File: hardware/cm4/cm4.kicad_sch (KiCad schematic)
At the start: 10 parts, among them J11 CM4 Stecker 1, J12 CM4 Stecker 2, Q10 BSS84

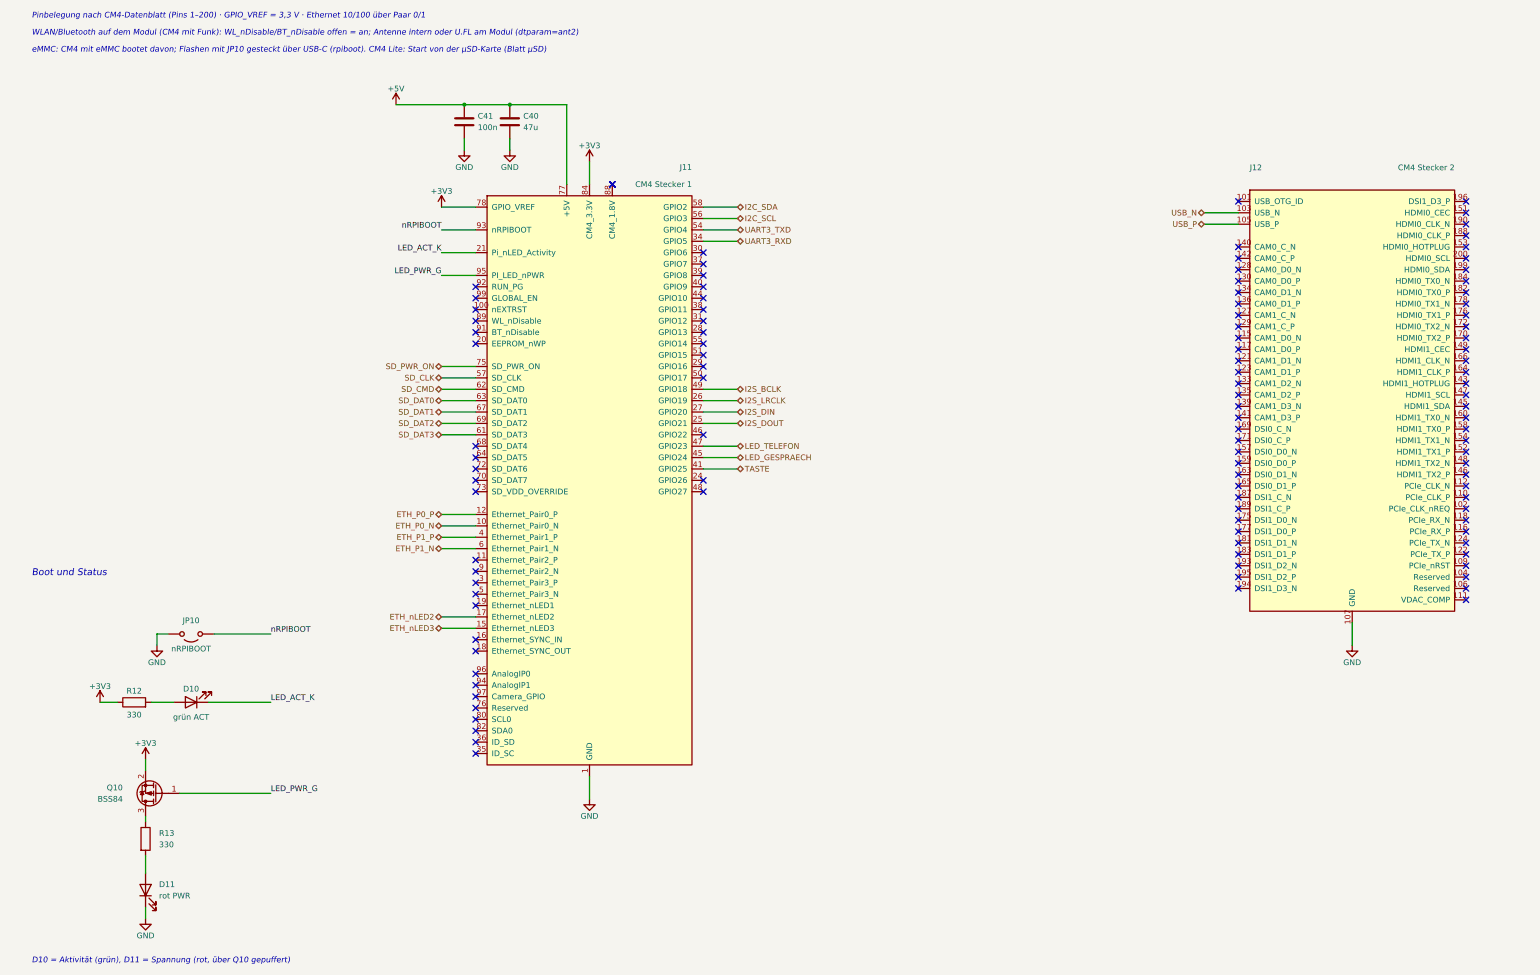
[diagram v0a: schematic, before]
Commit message: CM4-Träger 0.3: Leiterplatte (4 Lagen, JLCPCB), Ein/Aus-Taster, Lüfter, lieferbare Teile
Schaltplan
- Codec TI TLV320AIC3204 statt WM8731 (abgekündigt); MCLK 12 MHz, Reset GPIO26, I²C an GPIO0/1
- Ein/Aus-Taster an GPIO3 (gpio-shutdown im Betrieb, Bootloader-Wecken im Halt)
- Lüfterblatt: AO3400A an GPIO12, Freilaufdiode, JST-PH-Anschluss; gpio-fan über SoC-Temperatur
- Konfig-Taster SW2 und Status-LED D3; Würth RJ45/RJ12, Bourns SM-LP-5001, TPD4E05U06
- reproduzierbare UUIDs (Schaltplan ↔ Platine bleiben verknüpft), eigene Footprints in hardware/bibliothek

Leiterplatte (erzeuge_layout.py)
- 110 × 85 mm, F.Cu / In1 GND / In2 +3V3 / B.Cu, JLC04161H-7628, JLCPCB-Regeln (.kicad_dru)
- CM4-Lage nach CM4IO-Referenz, Antennen-Sperrzone, isolierte Bereiche GND_ISO/GNDA mit Trennstreifen
- eigenes Fanout zu den Ebenen, Routing mit FreeRouting 1.9.0 über xvfb (2.x: Telemetrie an)
- DRC ohne Verstöße, 0 offene Verbindungen, Schaltplan ↔ Platine identisch
- Bestellliste für Digikey mit geprüftem Lagerbestand
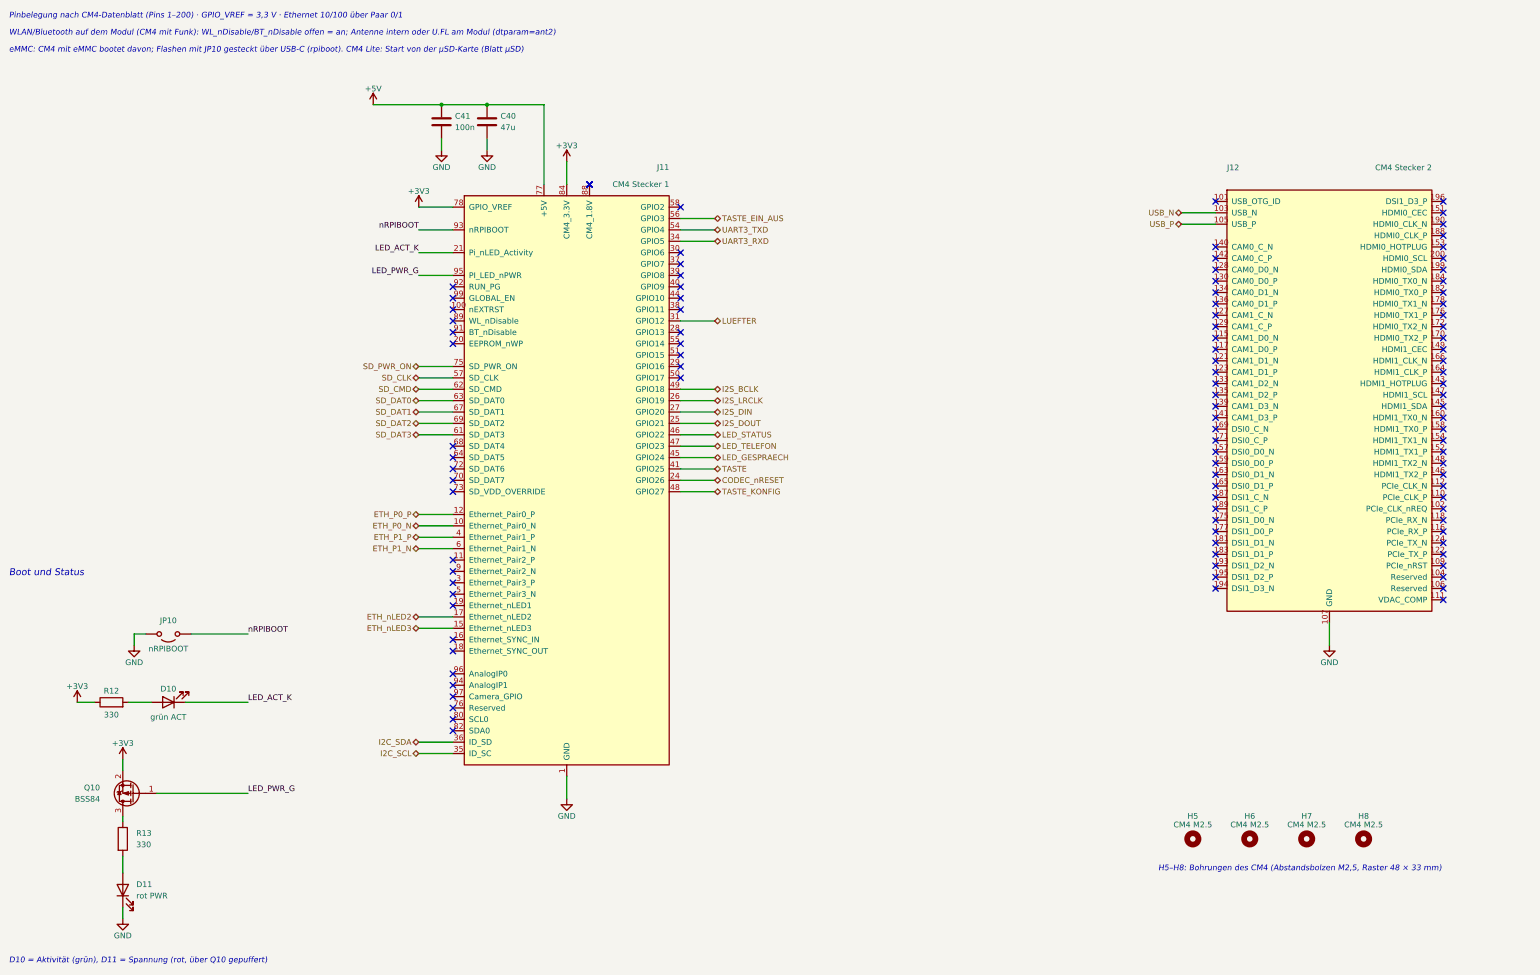
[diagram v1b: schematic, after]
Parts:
- added H5, H6, H7, H8: CM4 M2.5, MountingHole:MountingHole_2.7mm_M2.5, symbol Mechanical:MountingHole
- J12: footprint Connector_Hirose_DF40:Hirose_DF40C-100DS-0.4V_2x50_P0.4mm -> Sopho2SIP:Hirose_DF40C-100DS-0.4V_2x50_P0.4mm_Pins101-200
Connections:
- net I2C_SCL: now also J11.35 (ID_SC); no longer J11.56 (GPIO3)
- net I2C_SDA: now also J11.36 (ID_SD); no longer J11.58 (GPIO2)
- net CODEC_nRESET: now reaches J11.24 (GPIO26)
- net LUEFTER: now reaches J11.31 (GPIO12)
- net LED_STATUS: now reaches J11.46 (GPIO22)
- net TASTE_KONFIG: now reaches J11.48 (GPIO27)
- new net TASTE_EIN_AUS: J11.56 (GPIO3)
- no-connect marks 112 -> 107
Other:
- note added: "H5–H8: Bohrungen des CM4 (Abstandsbolzen M2,5, Raster 48 × 33 mm)"
